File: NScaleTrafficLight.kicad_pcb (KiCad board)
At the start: 2 copper layers, 4 x 11 mm, 10 parts, among them J1 Conn_01x01_Pin, J2 Conn_01x01_Pin, J3 Conn_01x01_Pin, J4 Conn_01x01_Pin

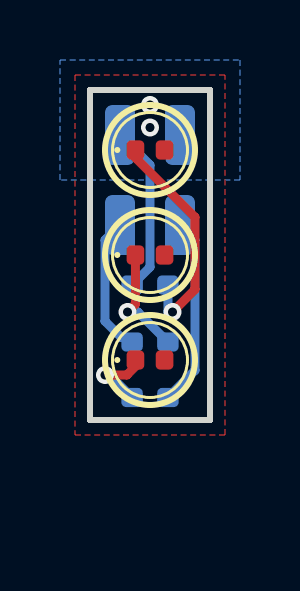
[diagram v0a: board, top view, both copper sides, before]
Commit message: Add resistor network, 4th signal light option
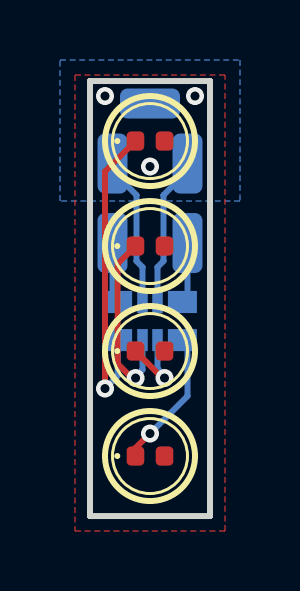
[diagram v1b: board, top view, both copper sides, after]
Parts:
- removed R1, R2, R3: 220R, Resistor_SMD:R_0402_1005Metric_Pad0.72x0.64mm_HandSolder
- added D4: Green, LED_SMD:LED_0402_1005Metric, F.Cu at (48.5, 53.5)
- added J5: Conn_01x01_Pin, Connector_Wire:SolderWirePad_1x01_SMD_1x2mm, B.Cu at (49.8, 46.4)
- added R4: EXB-28V221JX, footprints:EXB28V_PAN, B.Cu at (48.5, 49.0)
- moved J1 3.61 mm to (47.2, 46.4)
- moved J2 2.06 mm to (47.2, 43.8)
- moved J3 2.06 mm to (49.8, 43.8)
- moved J4 1.45 mm to (48.5, 41.8), turned to -90 degrees
- moved D1 0.30 mm to (48.5, 43.0)
- moved D2 0.30 mm to (48.5, 46.5)
- moved D3 0.30 mm to (48.5, 50.0)
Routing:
- net Net-(D4-K): track 0.00 -> 4.65 mm, vias 0 -> 1
- net Net-(J1-Pin_1): track 5.66 -> 2.04 mm
- net Net-(D1-K): track 7.44 -> 10.5 mm
- net Net-(D2-K): track 3.77 -> 6.26 mm
- net Net-(J5-Pin_1): track 0.00 -> 2.04 mm
- net Net-(J3-Pin_1): track 6.33 -> 4.78 mm
- net +3V3: vias 2 -> 3
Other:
- board size 4 x 11 mm -> 4 x 14.5 mm
